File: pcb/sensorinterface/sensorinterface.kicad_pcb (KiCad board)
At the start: 2 copper layers, 13 parts, among them J1 Conn_01x03, J2 Conn_01x03, J3 Conn_01x05, U1 LM393

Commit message: Add LEDs.
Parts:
- added C4: C, Capacitor_SMD:C_0603_1608Metric, F.Cu at (163.4, 110.4)
- added D1: LED, LED_SMD:LED_0603_1608Metric, F.Cu at (121.5, 120.7)
- added D2: LED, LED_SMD:LED_0603_1608Metric, F.Cu at (149.1, 120.7)
- added R7: 1k, Resistor_SMD:R_0603_1608Metric, F.Cu at (145.7, 120.7)
- added R8: 1k, Resistor_SMD:R_0603_1608Metric, F.Cu at (124.8, 120.7)
- R1, R2: value 1k -> 680

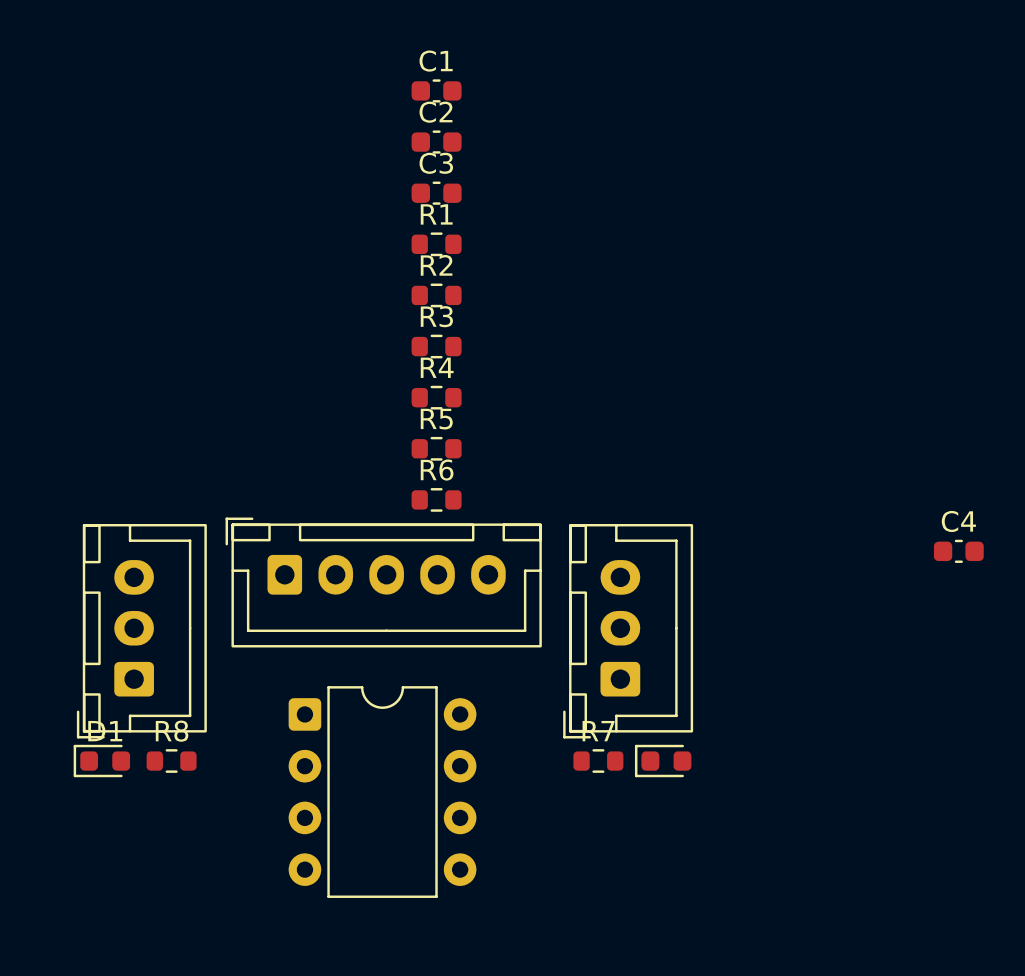
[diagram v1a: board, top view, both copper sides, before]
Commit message: Complete routing.
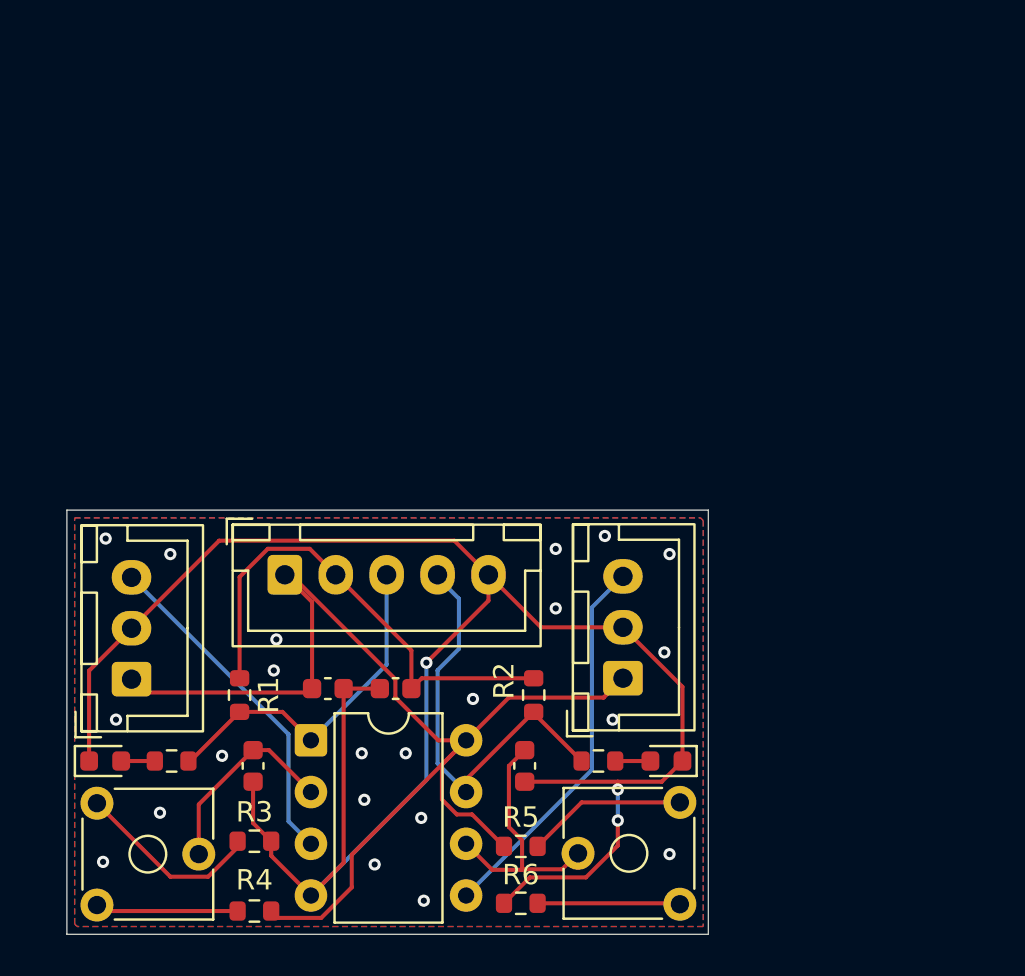
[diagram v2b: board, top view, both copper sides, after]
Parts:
- added RV1: 1k, Potentiometer_THT:Potentiometer_Trimmer_ACP_CA6v_Horizontal, F.Cu at (121.1, 127.7)
- added RV2: 1k, Potentiometer_THT:Potentiometer_Trimmer_ACP_CA6v_Horizontal, F.Cu at (149.7, 122.7)
- R3, R4, R5, R6: value R -> 2k
- moved C2 31.9 mm to (128.8, 120.9), turned to -90 degrees
- moved C1 29.8 mm to (132.4, 117.1)
- moved C4 28.5 mm to (135.8, 117.1), turned to 180 degrees
- moved C3 28.5 mm to (142.1, 120.9), turned to -90 degrees
- moved R4 26.7 mm to (128.8, 128.0), turned to 180 degrees
- moved R3 25.9 mm to (128.8, 124.6)
- moved R1 24.2 mm to (128.1, 117.4), turned to -90 degrees
- moved R6 20.2 mm to (141.9, 127.6), turned to 180 degrees
- moved R2 20.2 mm to (142.6, 117.4), turned to -90 degrees
- moved R5 20.0 mm to (141.9, 124.8)
- moved U1 1.30 mm to (131.6, 119.6)
- moved J2 0.14 mm to (146.9, 116.6)
- moved J1 0.13 mm to (122.8, 116.6)
- turned D2 to 180 degrees
- turned R8 to 180 degrees
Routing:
- net GND: track 0.00 -> 99.6 mm, vias 0 -> 25
- net +5V: track 0.00 -> 58.8 mm
- net +3.3V: track 0.00 -> 24.1 mm
- net Net-(J3-Pin_4): track 0.00 -> 20.8 mm
- net Net-(J2-Pin_3): track 0.00 -> 18.9 mm
- net Net-(J3-Pin_3): track 0.00 -> 17.3 mm
- net Net-(J1-Pin_3): track 0.00 -> 16.7 mm
- net Net-(U1B--): track 0.00 -> 12.8 mm
- net Net-(U1A--): track 0.00 -> 9.90 mm
- net Net-(R3-Pad1): track 0.00 -> 9.30 mm
- net Net-(R5-Pad2): track 0.00 -> 7.88 mm
- net Net-(R4-Pad2): track 0.00 -> 7.03 mm
- net Net-(R6-Pad1): track 0.00 -> 7.01 mm
- net Net-(D2-A): track 0.00 -> 1.73 mm
- net Net-(D1-A): track 0.00 -> 1.65 mm
- added copper zone on B.Cu, net GND
- added copper zone on F.Cu, net GND
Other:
- board outline added: 31.5 x 20.8 mm
